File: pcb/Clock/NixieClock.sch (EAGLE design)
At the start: 43 parts, among them IC1 74141N, IC2 MEGA8-P, IC3 7805L, J1 DC-8N, Q1 IRF710, Q2 32kHz

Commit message: Replaced backup capacitor with a CR1220 battery holder.
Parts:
- removed C14: 0.1F, rcl:CPOL-EUE5-13
- removed R5: 100, rcl:R-EU_0204/5
- added D5: BAT85, diode:1N4148DO35-7
- added U$3: BAT1220THT, WB:BAT1220THT
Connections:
- net GND: now also U$3.P$2; no longer C14.-
- net N$3: now also D5.A, U$3.P$1; no longer C14.+, R5.1
- net UC_VCC: now also D5.C; no longer R5.2
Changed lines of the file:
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@@
 <?xml version="1.0" encoding="utf-8"?>
 <!DOCTYPE eagle SYSTEM "eagle.dtd">
-<eagle version="6.3">
+<eagle version="6.6.0">
 <drawing>
 <settings>
@@
 <part name="C9" library="rcl" deviceset="C-EU" device="025-025X050" value="27pF"/>
 <part name="GND9" library="supply1" deviceset="GND" device=""/>
-<part name="C14" library="rcl" deviceset="CPOL-EU" device="E5-13" value="0.1F"/>
 <part name="D2" library="diode" deviceset="1N4148" device="DO35-7" value="BAT85"/>
 <part name="C8" library="rcl" deviceset="C-EU" device="050-025X075" value="100nF"/>
@@
 <part name="FRAME1" library="frames" deviceset="A4L-LOC" device=""/>
 <part name="Q1" library="transistor-power" deviceset="PMOSFET_N" device="TO220BH" value="IRF710"/>
-<part name="R5" library="rcl" deviceset="R-EU_" device="0204/5" value="100"/>
 <part name="C5" library="Various" deviceset="CPOL-EU" device="" value="4.7uF/250V"/>
 <part name="JP4" library="pinhead" deviceset="PINHD-1X6" device="/90"/>
@@
 <part name="R9" library="rcl" deviceset="R-EU_" device="0204/5" value="10"/>
 <part name="V2" library="supply2" deviceset="VCC" device=""/>
+<part name="U$3" library="WB" deviceset="BAT1220THT" device=""/>
+<part name="D5" library="diode" deviceset="1N4148" device="DO35-7" value="BAT85"/>
 </parts>
 <sheets>
@@
 <instance part="C9" gate="G$1" x="15.24" y="203.2" rot="R90"/>
 <instance part="GND9" gate="1" x="-7.62" y="111.76"/>
-<instance part="C14" gate="G$1" x="-144.78" y="147.32"/>
 <instance part="D2" gate="G$1" x="-157.48" y="160.02"/>
 <instance part="C8" gate="G$1" x="193.04" y="210.82" rot="R180"/>
@@
 <instance part="FRAME1" gate="G$1" x="-33.02" y="78.74"/>
 <instance part="Q1" gate="G$1" x="-187.96" y="208.28"/>
-<instance part="R5" gate="G$1" x="-144.78" y="154.94" rot="R90"/>
 <instance part="C5" gate="G$1" x="-157.48" y="213.36" smashed="yes">
 <attribute name="NAME" x="-155.1686" y="205.867" size="1.778" layer="95" rot="R90"/>
@@
 <instance part="R9" gate="G$1" x="-200.66" y="205.74" rot="R180"/>
 <instance part="V2" gate="G$1" x="2.54" y="246.38"/>
+<instance part="U$3" gate="G$1" x="-144.78" y="149.86"/>
+<instance part="D5" gate="G$1" x="-144.78" y="154.94" rot="R90"/>
 </instances>
 <busses>
@@
 <pinref part="C12" gate="G$1" pin="1"/>
 <pinref part="C11" gate="G$1" pin="-"/>
-<pinref part="C14" gate="G$1" pin="-"/>
 <pinref part="J1" gate="G$1" pin="3"/>
 <wire x1="-215.9" y1="152.4" x2="-213.36" y2="152.4" width="0.1524" layer="91"/>
@@
 <wire x1="-213.36" y1="149.86" x2="-213.36" y2="152.4" width="0.1524" layer="91"/>
 <junction x="-213.36" y="152.4"/>
+<wire x1="-144.78" y1="142.24" x2="-144.78" y2="143.51" width="0.1524" layer="91"/>
+<pinref part="U$3" gate="G$1" pin="P$2"/>
 </segment>
 <segment>
@@
 <label x="-139.7" y="160.02" size="1.27" layer="95" xref="yes"/>
 <pinref part="D2" gate="G$1" pin="C"/>
-<pinref part="R5" gate="G$1" pin="2"/>
+<pinref part="D5" gate="G$1" pin="C"/>
 <wire x1="-144.78" y1="160.02" x2="-139.7" y2="160.02" width="0.1524" layer="91"/>
+<wire x1="-144.78" y1="157.48" x2="-144.78" y2="160.02" width="0.1524" layer="91"/>
 <junction x="-144.78" y="160.02"/>
 </segment>
@@
 <pinref part="R7" gate="G$1" pin="1"/>
 <pinref part="R8" gate="G$1" pin="2"/>
-</segment>
-</net>
-<net name="N$3" class="0">
-<segment>
-<pinref part="R5" gate="G$1" pin="1"/>
-<pinref part="C14" gate="G$1" pin="+"/>
 </segment>
 </net>
@@
 </segment>
 </net>
+<net name="N$3" class="0">
+<segment>
+<pinref part="U$3" gate="G$1" pin="P$1"/>
+<pinref part="D5" gate="G$1" pin="A"/>
+</segment>
+</net>

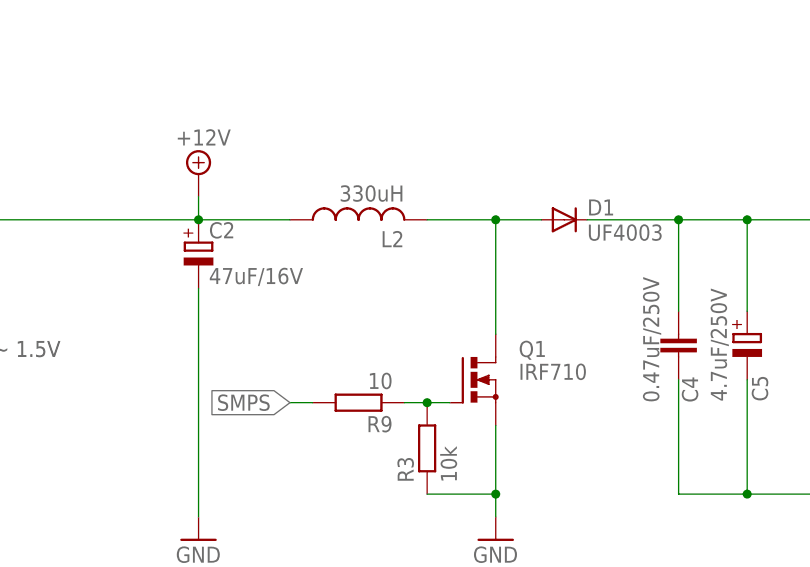
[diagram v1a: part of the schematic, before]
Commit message: Changed MOSFET from IRF710 to IRF740. Added part number for inductor
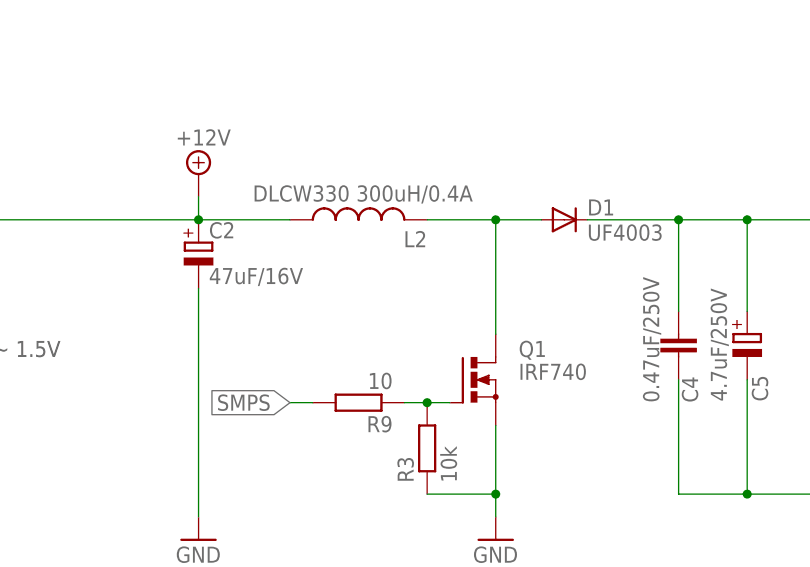
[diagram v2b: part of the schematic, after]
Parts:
- L2: value 330uH -> DLCW330 300uH/0.4A
- Q1: value IRF710 -> IRF740
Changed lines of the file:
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@@
 <part name="V1" library="supply2" deviceset="VCC" device=""/>
 <part name="C4" library="capacitor-wima" deviceset="C" device="10/6" value="0.47uF/250V"/>
-<part name="L2" library="WB" deviceset="RADIAL-CHOKE" device="4MM" value="330uH"/>
+<part name="L2" library="WB" deviceset="RADIAL-CHOKE" device="4MM" value="DLCW330 300uH/0.4A"/>
 <part name="FRAME1" library="frames" deviceset="A4L-LOC" device=""/>
-<part name="Q1" library="transistor-power" deviceset="PMOSFET_N" device="TO220BH" value="IRF710"/>
+<part name="Q1" library="transistor-power" deviceset="PMOSFET_N" device="TO220BH" value="IRF740"/>
 <part name="C5" library="Various" deviceset="CPOL-EU" device="" value="4.7uF/250V"/>
 <part name="JP4" library="pinhead" deviceset="PINHD-1X6" device="/90"/>
@@
 <attribute name="VALUE" x="-167.259" y="205.74" size="1.778" layer="96" rot="R90"/>
 </instance>
-<instance part="L2" gate="G$1" x="-200.66" y="226.06" rot="R90"/>
+<instance part="L2" gate="G$1" x="-200.66" y="226.06" smashed="yes" rot="R90">
+<attribute name="NAME" x="-193.04" y="224.79" size="1.778" layer="95" rot="R180"/>
+<attribute name="VALUE" x="-187.96" y="229.87" size="1.778" layer="96" rot="R180"/>
+</instance>
 <instance part="FRAME1" gate="G$1" x="-33.02" y="78.74"/>
 <instance part="Q1" gate="G$1" x="-187.96" y="208.28"/>

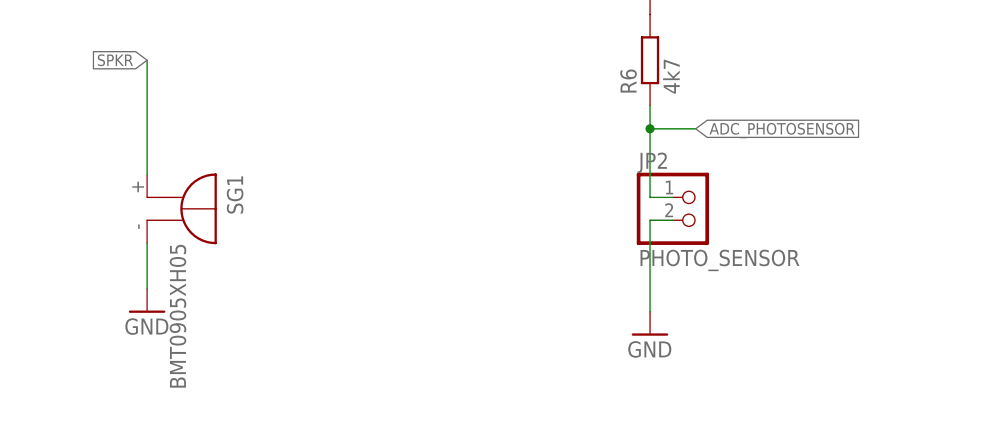
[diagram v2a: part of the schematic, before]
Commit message: Added part number for photoresistor
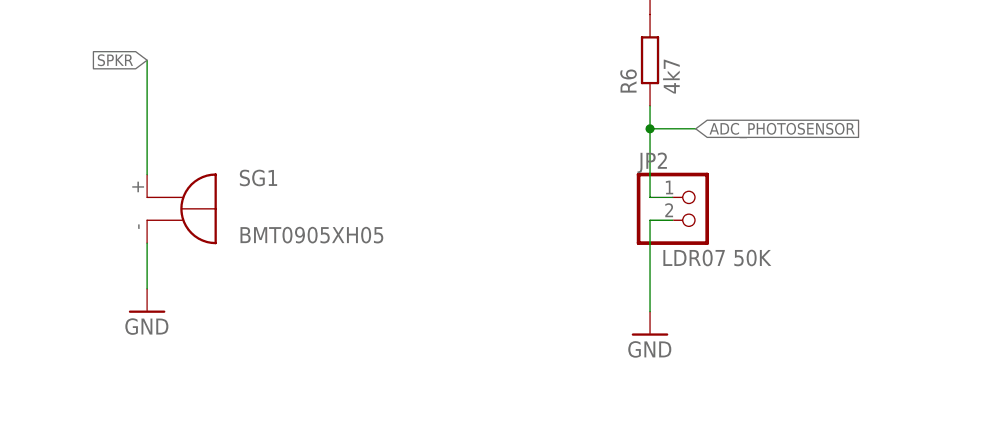
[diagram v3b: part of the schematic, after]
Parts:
- JP2: value PHOTO_SENSOR -> LDR07 50K
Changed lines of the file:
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@@
 <part name="V10" library="supply2" deviceset="VCC" device=""/>
 <part name="GND11" library="supply1" deviceset="GND" device=""/>
-<part name="JP2" library="pinhead" deviceset="PINHD-1X2" device="" value="PHOTO_SENSOR"/>
+<part name="JP2" library="pinhead" deviceset="PINHD-1X2" device="" value="LDR07 50K"/>
 <part name="V12" library="supply2" deviceset="VCC" device=""/>
 <part name="GND10" library="supply1" deviceset="GND" device=""/>
@@
 <instance part="V10" gate="G$1" x="-162.56" y="162.56"/>
 <instance part="GND11" gate="1" x="-12.7" y="205.74"/>
-<instance part="JP2" gate="G$1" x="53.34" y="121.92"/>
+<instance part="JP2" gate="G$1" x="53.34" y="121.92" smashed="yes">
+<attribute name="NAME" x="46.99" y="127.635" size="1.778" layer="95"/>
+<attribute name="VALUE" x="49.53" y="116.84" size="1.778" layer="96"/>
+</instance>
 <instance part="V12" gate="G$1" x="48.26" y="147.32" rot="MR0"/>
 <instance part="GND10" gate="1" x="48.26" y="109.22"/>
@@
 <instance part="R3" gate="G$1" x="-193.04" y="200.66" rot="R90"/>
 <instance part="J1" gate="G$1" x="-223.52" y="152.4"/>
-<instance part="SG1" gate="G$1" x="-5.08" y="124.46" rot="R270"/>
+<instance part="SG1" gate="G$1" x="-5.08" y="124.46" smashed="yes" rot="R270">
+<attribute name="NAME" x="2.54" y="125.73" size="1.778" layer="95"/>
+<attribute name="VALUE" x="2.54" y="119.38" size="1.778" layer="96"/>
+</instance>
 <instance part="D3" gate="G$1" x="-124.46" y="218.44" rot="R90"/>
 <instance part="D4" gate="G$1" x="-124.46" y="203.2" rot="R90"/>
